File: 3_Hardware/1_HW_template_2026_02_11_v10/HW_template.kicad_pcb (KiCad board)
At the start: 4 copper layers, 63.5 x 118.1 mm, 89 parts, among them J1 AudioJack3, P1 type="R" model="Conn_01x32_Fe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, P2 type="R" model="Conn_01x32_Fe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, U1 MCP6002-xSN, U2 MCP6002-xSN, U3 MCP6002-xSN, U4 LD1117S33TR_SOT223, U5 AD8232ACPZ-R7, Y1 OpenLog, Y2 Radar K-LC5-RFB-00C

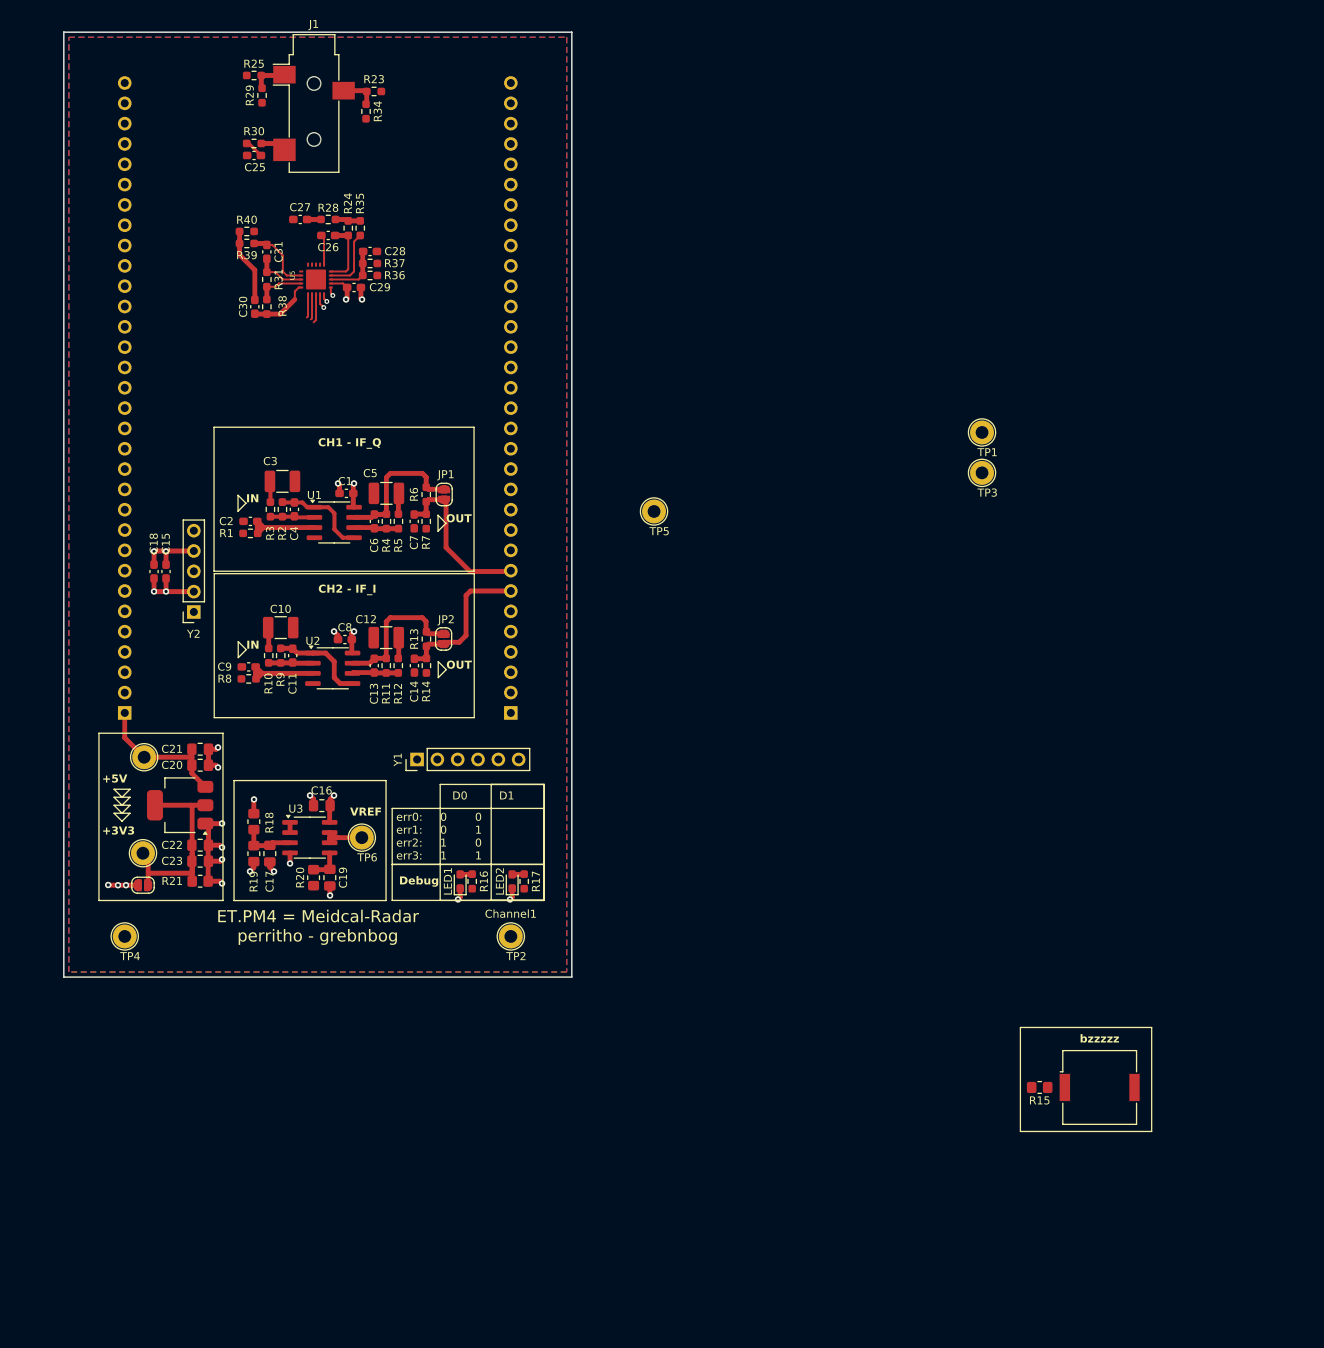
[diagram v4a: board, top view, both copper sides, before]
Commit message: updated layout
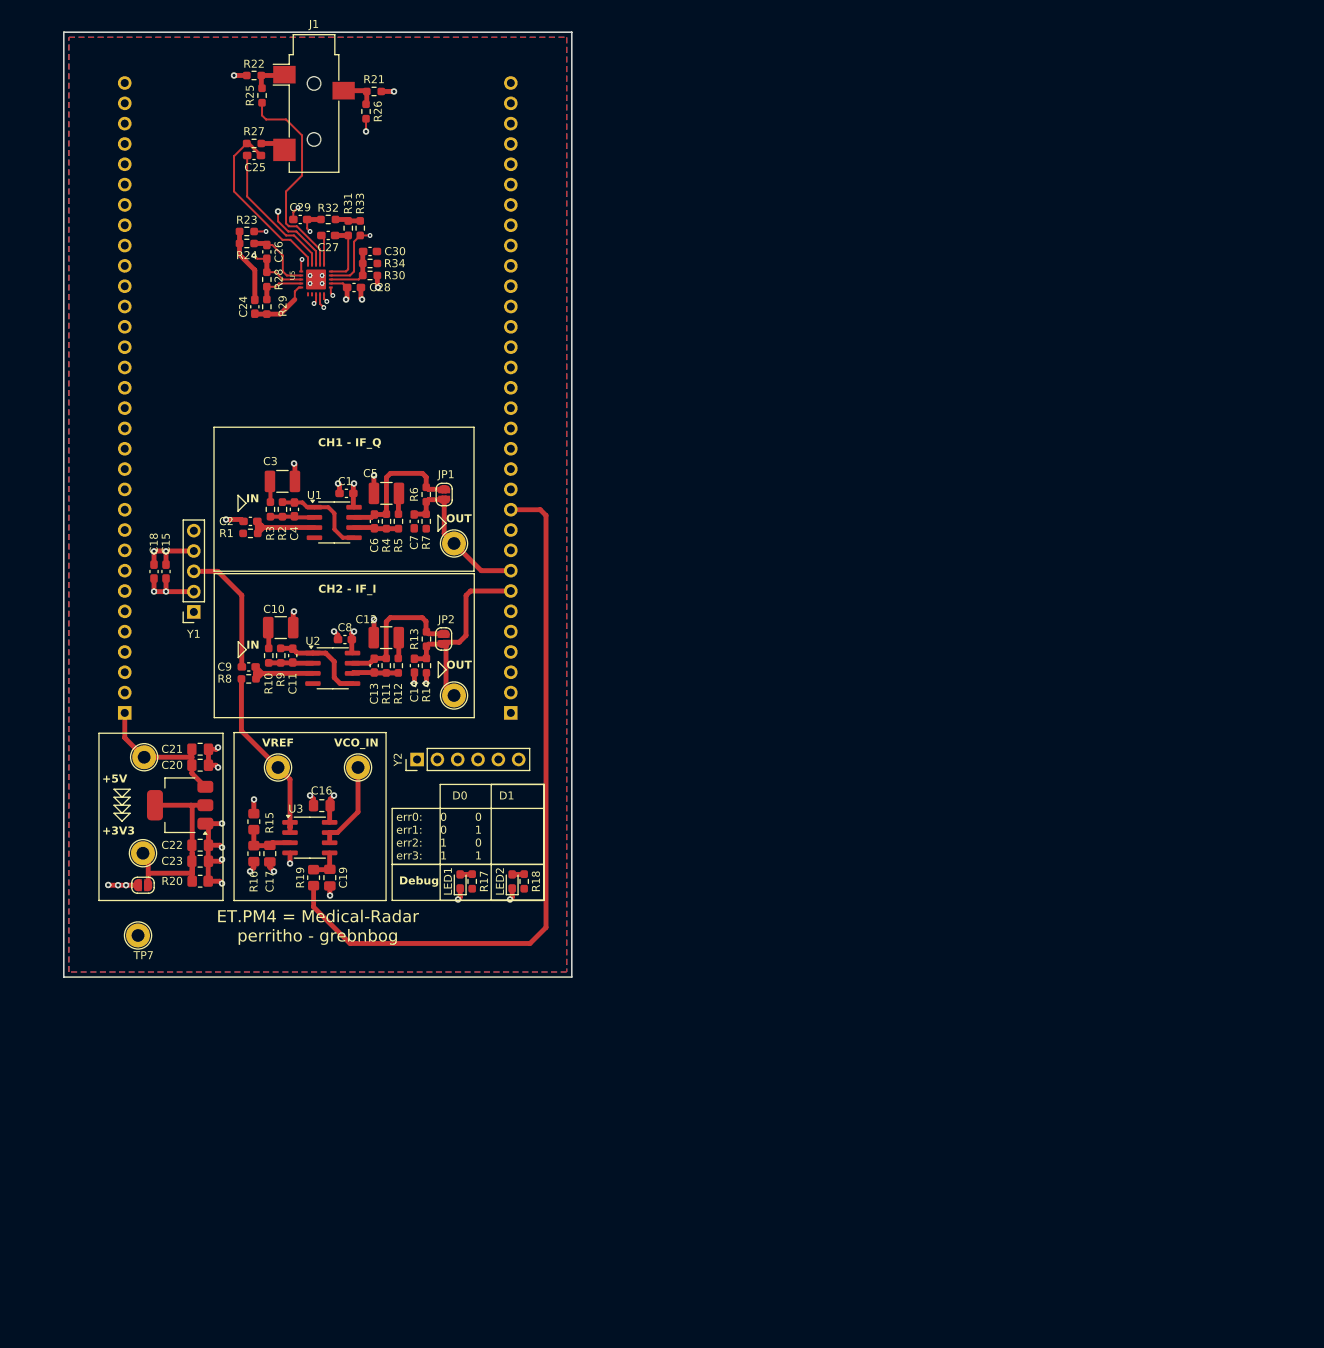
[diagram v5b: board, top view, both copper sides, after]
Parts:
- removed BZ1: Buzzer_Piezo, Buzzer_Beeper:Buzzer_Murata_PKMCS0909E
- removed the R15 at (167.7, 153.5)
- removed the TP5 at (119.5, 81.5)
- removed the TP6 at (83.0, 122.3)
- added TP7: ~, TestPoint:TestPoint_Loop_D2.60mm_Drill1.6mm_Beaded, F.Cu at (55.0, 134.5)
- TP4: value ~ -> Channel1
- moved TP1 88.5 mm to (82.5, 113.5), turned to -90 degrees
- moved TP3 66.6 mm to (94.5, 85.5)
- moved TP2 30.9 mm to (94.5, 104.5)
- moved TP4 28.5 mm to (72.5, 113.5), turned to -90 degrees
- renumbered C30 to C24, C31 to C26, C26 to C27, C29 to C28, C27 to C29, C28 to C30, R18 to R15, R19 to R16, R16 to R17, R17 to R18, R20 to R19, R21 to R20, R23 to R21, R25 to R22, R40 to R23, R39 to R24, R29 to R25, R34 to R26, R30 to R27, R31 to R28, R38 to R29, R36 to R30, R24 to R31, R28 to R32, R35 to R33, R37 to R34, TP7 to TP5, TP8 to TP6, Y2 to Y1, Y1 to Y2
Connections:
- TP4 pad 1: GND -> Vref
- U5 pad 11: /ECG/LO- -> unconnected-(U5-LO--Pad11)
- U5 pad 12: /ECG/LO+ -> unconnected-(U5-LO+-Pad12)
- U5 pad 13: /ECG/SDN -> 3V3_INT
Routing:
- net PA5: track 0.00 -> 90.6 mm
- net /Analog/VCO_in: track 7.51 -> 60.8 mm
- net +5V: track 17.9 -> 64.7 mm
- net Net-(U5-+IN): track 0.00 -> 26.9 mm
- net Net-(U5--IN): track 0.00 -> 25.9 mm, vias 0 -> 2
- net Vref: track 1.27 -> 22.4 mm
- net Net-(U5-RLD): track 2.40 -> 22.6 mm
- net Net-(U5-RLDFB): track 0.00 -> 17.6 mm
- net IF_Q: track 0.00 -> 17.2 mm, vias 0 -> 1
- net Net-(U5-IAOUT): track 7.93 -> 25.0 mm, vias 0 -> 2
- net IF_I: track 0.00 -> 16.2 mm
- net GND: track 44.6 -> 59.6 mm, vias 20 -> 30
- net REFOUT: track 6.35 -> 20.0 mm, vias 0 -> 2
- net Net-(U5-SW): track 1.72 -> 8.83 mm, vias 0 -> 2
- net PC1: track 19.5 -> 26.5 mm
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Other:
- board text added: "ET.PM4 = Medical-Radar perritho - grebnbog"
- board text added: "VCO_IN"
- board text removed: "ET.PM4 = Meidcal-Radar perritho - grebnbog"
- board text removed: "bzzzzz"

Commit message: pcb schematics finished + layout
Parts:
- moved R23 0.19 mm to (68.4, 46.5)
- moved R24 0.19 mm to (68.4, 48.0)
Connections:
- C24 pad 1: /ECG/sig_out -> PF6
- R17 pad 1: D0 -> PE5
- R18 pad 1: D1 -> PE3
- R29 pad 2: /ECG/sig_out -> PF6
- U5 pad 10: /ECG/sig_out -> PF6
- Y2 pad 1: PE6 -> unconnected-(Y2-GRN-Pad1)
- Y2 pad 2: PA9 -> PG14_
- Y2 pad 3: PA10 -> unconnected-(Y2-TXO-Pad3)
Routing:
- net PE3: track 0.00 -> 103.2 mm, vias 0 -> 1
- net PE5: track 0.00 -> 91.2 mm, vias 0 -> 1
- net PG14_: track 0.00 -> 78.9 mm
- net PF6: track 0.00 -> 77.3 mm, vias 0 -> 1
- net Vref: track 22.4 -> 43.2 mm, vias 0 -> 2
- net /ECG/sig_out: track 7.78 -> 0.00 mm
- net GND: track 59.6 -> 64.2 mm, vias 30 -> 32
- net 3V3_INT: track 34.1 -> 36.6 mm
- net Net-(U5-SW): track 8.83 -> 10.2 mm
- net REFOUT: track 20.0 -> 20.6 mm
- net Net-(U5-RLD): track 22.6 -> 22.1 mm
